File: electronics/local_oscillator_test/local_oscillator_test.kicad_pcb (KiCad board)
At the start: 2 copper layers, 0 parts

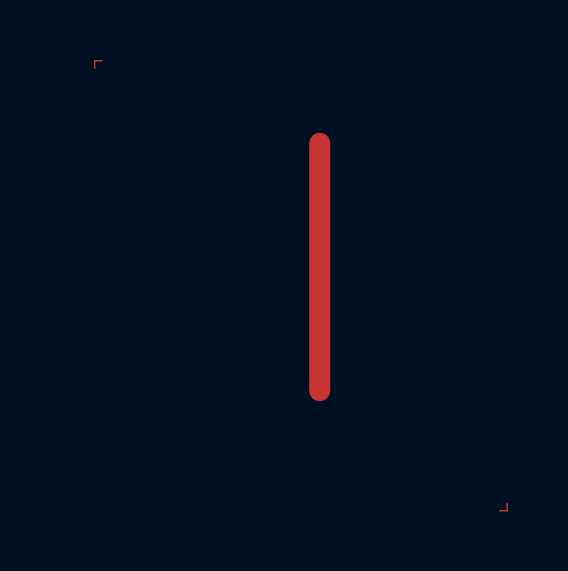
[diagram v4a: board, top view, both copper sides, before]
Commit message: Impulse functional, just needed to set ground plane
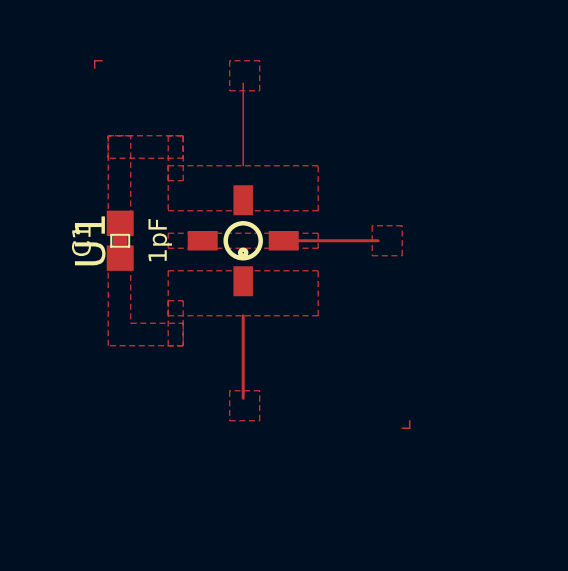
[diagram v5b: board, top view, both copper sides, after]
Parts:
- added C1: 1pF, 0402, F.Cu at (15.8, 18.5)
- added U1: CE3520K3, 0xDBFB7:4-Micro-X, F.Cu at (19.9, 18.5)
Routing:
- net (no net): track 9.25 -> 1.00 mm
- net /GATE: track 0.00 -> 3.91 mm
- net GND: track 0.00 -> 2.75 mm
- net /OSC1: track 0.00 -> 2.75 mm
- added copper zone on F.Cu, net /GATE
- added copper zone on F.Cu, net /OSC1
- added copper zone on F.Cu, net GND
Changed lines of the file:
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@@
     (thickness 1.6)
     (drawings 0)
-    (tracks 5)
+    (tracks 8)
     (zones 0)
-    (modules 0)
-    (nets 1)
+    (modules 2)
+    (nets 4)
   )
   (page A4)
@@
   )
   (net 0 "")
+  (net 1 /OSC1)
+  (net 2 GND)
+  (net 3 /GATE)
   (net_class Default "This is the default net class."
     (clearance 0.2)
@@
     (uvia_dia 0.3)
     (uvia_drill 0.1)
+    (add_net /GATE)
+    (add_net /OSC1)
+    (add_net GND)
+  )
+  (module 0xDBFB7:4-Micro-X (layer F.Cu)
+    (at 19.95 18.5 270)
+    (fp_text reference U1 (at 0 5.072 270) (layer F.SilkS)
+      (effects (font (size 1 1) (thickness 0.15)))
+    )
+    (fp_text value CE3520K3 (at 0 4.072 270) (layer F.Fab)
+      (effects (font (size 1 1) (thickness 0.15)))
+    )
+    (fp_text user Gate (at 1.4 -0.5 270) (layer Dwgs.User)
+      (effects (font (size 0.2 0.2) (thickness 0.05)))
+    )
+    (fp_text user Drain (at -1.3 -0.5 270) (layer Dwgs.User)
+      (effects (font (size 0.2 0.2) (thickness 0.05)))
+    )
+    (fp_text user Source (at -0.5 -1.3) (layer Dwgs.User)
+      (effects (font (size 0.2 0.2) (thickness 0.05)))
+    )
+    (fp_text user Source (at -0.5 1.4) (layer Dwgs.User)
+      (effects (font (size 0.2 0.2) (thickness 0.05)))
+    )
+    (fp_circle (center 0 0) (end 0.583095 0) (layer F.SilkS) (width 0.15))
+    (fp_circle (center 0.4 0) (end 0.5 0) (layer F.SilkS) (width 0.15))
+    (pad 2 smd rect (at -1.35 0) (size 0.65 1) (layers F.Cu F.Paste F.Mask)
+      (net 3 /GATE))
+    (pad 1 smd rect (at 0 -1.35 270) (size 0.65 1) (layers F.Cu F.Paste F.Mask)
+      (net 2 GND))
+    (pad 4 smd rect (at 1.35 0 180) (size 0.65 1) (layers F.Cu F.Paste F.Mask)
+      (net 3 /GATE))
+    (pad 3 smd rect (at 0 1.35 90) (size 0.65 1) (layers F.Cu F.Paste F.Mask)
+      (net 2 GND))
+  )
+  (module 0402 (layer F.Cu)
+    (at 15.85 18.5 90)
+    (descr "GENERIC 1005 (0402) PACKAGE")
+    (tags "GENERIC 1005 (0402) PACKAGE")
+    (attr smd)
+    (fp_text reference C1 (at 0 -1.27 90) (layer F.SilkS)
+      (effects (font (size 0.6096 0.6096) (thickness 0.127)))
+    )
+    (fp_text value 1pF (at 0 1.27 90) (layer F.SilkS)
+      (effects (font (size 0.6096 0.6096) (thickness 0.127)))
+    )
+    (fp_line (start -0.55372 0.3048) (end -0.254 0.3048) (layer Dwgs.User) (width 0.06604))
+    (fp_line (start -0.254 0.3048) (end -0.254 -0.3048) (layer Dwgs.User) (width 0.06604))
+    (fp_line (start -0.55372 -0.3048) (end -0.254 -0.3048) (layer Dwgs.User) (width 0.06604))
+    (fp_line (start -0.55372 0.3048) (end -0.55372 -0.3048) (layer Dwgs.User) (width 0.06604))
+    (fp_line (start 0.25654 0.3048) (end 0.5588 0.3048) (layer Dwgs.User) (width 0.06604))
+    (fp_line (start 0.5588 0.3048) (end 0.5588 -0.3048) (layer Dwgs.User) (width 0.06604))
+    (fp_line (start 0.25654 -0.3048) (end 0.5588 -0.3048) (layer Dwgs.User) (width 0.06604))
+    (fp_line (start 0.25654 0.3048) (end 0.25654 -0.3048) (layer Dwgs.User) (width 0.06604))
+    (fp_line (start -0.19812 0.29972) (end 0.19812 0.29972) (layer F.SilkS) (width 0.06604))
+    (fp_line (start 0.19812 0.29972) (end 0.19812 -0.29972) (layer F.SilkS) (width 0.06604))
+    (fp_line (start -0.19812 -0.29972) (end 0.19812 -0.29972) (layer F.SilkS) (width 0.06604))
+    (fp_line (start -0.19812 0.29972) (end -0.19812 -0.29972) (layer F.SilkS) (width 0.06604))
+    (fp_line (start -0.26924 -0.2286) (end 0.26924 -0.2286) (layer Dwgs.User) (width 0.1524))
+    (fp_line (start 0.26924 0.2286) (end -0.26924 0.2286) (layer Dwgs.User) (width 0.1524))
+    (fp_line (start -1.19888 -0.6477) (end 1.19888 -0.6477) (layer F.CrtYd) (width 0.0508))
+    (fp_line (start 1.19888 -0.6477) (end 1.19888 0.6477) (layer F.CrtYd) (width 0.0508))
+    (fp_line (start 1.19888 0.6477) (end -1.19888 0.6477) (layer F.CrtYd) (width 0.0508))
+    (fp_line (start -1.19888 0.6477) (end -1.19888 -0.6477) (layer F.CrtYd) (width 0.0508))
+    (pad 1 smd rect (at -0.57912 0 90) (size 0.84836 0.89916) (layers F.Cu F.Paste F.Mask)
+      (net 3 /GATE) (solder_mask_margin 0.1016))
+    (pad 2 smd rect (at 0.57912 0 90) (size 0.84836 0.89916) (layers F.Cu F.Paste F.Mask)
+      (net 3 /GATE) (solder_mask_margin 0.1016))
   )
   (segment (start 15 12.75) (end 15 12.5) (width 0.05) (layer F.Cu) (net 0))
   (segment (start 15 12.5) (end 15.25 12.5) (width 0.05) (layer F.Cu) (net 0))
-  (segment (start 28.75 27.25) (end 28.75 27.5) (width 0.05) (layer F.Cu) (net 0))
-  (segment (start 28.75 27.5) (end 28.5 27.5) (width 0.05) (layer F.Cu) (net 0))
-  (segment (start 22.5 15.25) (end 22.5 23.5) (width 0.7) (layer F.Cu) (net 0))
+  (segment (start 25.5 24.5) (end 25.5 24.75) (width 0.05) (layer F.Cu) (net 0))
+  (segment (start 25.5 24.75) (end 25.25 24.75) (width 0.05) (layer F.Cu) (net 0))
+  (segment (start 19.95 13.25) (end 19.95 16) (width 0.05) (layer F.Cu) (net 1))
+  (segment (start 24.45 18.5) (end 21.7 18.5) (width 0.1) (layer F.Cu) (net 2))
+  (segment (start 19.95 21) (end 19.95 23.75) (width 0.1) (layer F.Cu) (net 3))
+  (segment (start 15.85 17.92088) (end 15.85 19.07912) (width 0.5) (layer F.Cu) (net 3))
+  (zone (net 3) (net_name /GATE) (layer F.Cu) (hatch edge 0.508)
+    (connect_pads yes (clearance 0))
+    (min_thickness 0.254)
+    (fill yes (arc_segments 16) (thermal_gap 0) (thermal_bridge_width 0))
+    (polygon
+      (pts
+        (xy 15.45 15) (xy 15.45 18) (xy 16.2 18) (xy 16.2 15)
+      )
+    )
+  )
+  (zone (net 1) (net_name /OSC1) (layer F.Cu) (hatch edge 0.508)
+    (connect_pads yes (clearance 0))
+    (min_thickness 0.254)
+    (fill yes (arc_segments 16) (thermal_gap 0) (thermal_bridge_width 0))
+    (polygon
+      (pts
+        (xy 19.5 13.5) (xy 20.5 13.5) (xy 20.5 12.5) (xy 19.5 12.5)
+      )
+    )
+  )
+  (zone (net 1) (net_name /OSC1) (layer F.Cu) (hatch edge 0.508)
+    (connect_pads yes (clearance 0))
+    (min_thickness 0.254)
+    (fill yes (arc_segments 16) (thermal_gap 0) (thermal_bridge_width 0))
+    (polygon
+      (pts
+        (xy 17.95 16.5) (xy 17.95 15) (xy 17.45 15) (xy 17.45 16.5)
+      )
+    )
+  )
+  (zone (net 3) (net_name /GATE) (layer F.Cu) (hatch edge 0.508)
+    (connect_pads yes (clearance 0))
+    (min_thickness 0.254)
+    (fill yes (arc_segments 16) (thermal_gap 0) (thermal_bridge_width 0))
+    (polygon
+      (pts
+        (xy 17.95 22) (xy 15.45 22) (xy 15.45 19) (xy 16.2 19) (xy 16.2 21.25)
+        (xy 17.95 21.25)
+      )
+    )
+  )
+  (zone (net 2) (net_name GND) (layer F.Cu) (hatch edge 0.508)
+    (connect_pads yes (clearance 0))
+    (min_thickness 0.254)
+    (fill yes (arc_segments 16) (thermal_gap 0) (thermal_bridge_width 0))
+    (polygon
+      (pts
+        (xy 24.25 18) (xy 24.25 19) (xy 25.25 19) (xy 25.25 18)
+      )
+    )
+  )
+  (zone (net 2) (net_name GND) (layer F.Cu) (hatch edge 0.508)
+    (connect_pads yes (clearance 0))
+    (min_thickness 0.254)
+    (fill yes (arc_segments 16) (thermal_gap 0) (thermal_bridge_width 0))
+    (polygon
+      (pts
+        (xy 17.45 18.25) (xy 22.45 18.25) (xy 22.45 18.75) (xy 17.45 18.75)
+      )
+    )
+  )
+  (zone (net 1) (net_name /OSC1) (layer F.Cu) (hatch edge 0.508)
+    (connect_pads yes (clearance 0))
+    (min_thickness 0.254)
+    (fill yes (arc_segments 16) (thermal_gap 0) (thermal_bridge_width 0))
+    (polygon
+      (pts
+        (xy 17.95 15) (xy 17.95 15.75) (xy 15.45 15.75) (xy 15.45 15)
+      )
+    )
+  )
+  (zone (net 3) (net_name /GATE) (layer F.Cu) (hatch edge 0.508)
+    (connect_pads yes (clearance 0))
+    (min_thickness 0.254)
+    (fill yes (arc_segments 16) (thermal_gap 0) (thermal_bridge_width 0))
+    (polygon
+      (pts
+        (xy 20.5 23.5) (xy 19.5 23.5) (xy 19.5 24.5) (xy 20.5 24.5)
+      )
+    )
+  )
+  (zone (net 3) (net_name /GATE) (layer F.Cu) (hatch edge 0.508)
+    (connect_pads yes (clearance 0))
+    (min_thickness 0.254)
+    (fill yes (arc_segments 16) (thermal_gap 0) (thermal_bridge_width 0))
+    (polygon
+      (pts
+        (xy 17.95 20.5) (xy 17.95 22) (xy 17.45 22) (xy 17.45 20.5)
+      )
+    )
+  )
+  (zone (net 3) (net_name /GATE) (layer F.Cu) (hatch edge 0.508)
+    (connect_pads yes (clearance 0.508))
+    (min_thickness 0.254)
+    (fill yes (arc_segments 16) (thermal_gap 0.508) (thermal_bridge_width 0.508))
+    (polygon
+      (pts
+        (xy 22.45 21) (xy 22.45 19.5) (xy 17.45 19.5) (xy 17.45 21)
+      )
+    )
+  )
+  (zone (net 3) (net_name /GATE) (layer F.Cu) (hatch edge 0.508)
+    (connect_pads yes (clearance 0.508))
+    (min_thickness 0.254)
+    (fill yes (arc_segments 16) (thermal_gap 0.508) (thermal_bridge_width 0.508))
+    (polygon
+      (pts
+        (xy 22.45 17.5) (xy 22.45 16) (xy 17.45 16) (xy 17.45 17.5)
+      )
+    )
+  )
 )

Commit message: LO works!
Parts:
- added C2: 1pF, 0402, F.Cu at (17.0, 15.5)
- moved U1 3.38 mm to (23.2, 19.2)
- moved C1 2.45 mm to (18.2, 18.0)
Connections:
- C1 pad 2: /GATE -> Net-(C1-Pad2)
- U1 pad 2: /GATE -> /OSC1
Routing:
- net /GATE: track 3.91 -> 0.00 mm
- net GND: track 2.75 -> 0.00 mm
- net /OSC1: track 2.75 -> 0.00 mm
- removed copper zone on F.Cu, net /GATE
- removed copper zone on F.Cu, net /OSC1
- removed copper zone on F.Cu, net GND
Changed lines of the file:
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@@
     (thickness 1.6)
     (drawings 0)
-    (tracks 8)
+    (tracks 4)
     (zones 0)
-    (modules 2)
-    (nets 4)
+    (modules 3)
+    (nets 7)
   )
   (page A4)
@@
     (pad_drill 0.762)
     (pad_to_mask_clearance 0.2)
-    (aux_axis_origin 22.5 25)
-    (grid_origin 22.5 25)
+    (aux_axis_origin 15 12.5)
+    (grid_origin 15 12.5)
     (visible_elements FEFFFF7F)
     (pcbplotparams
@@
   )
   (net 0 "")
-  (net 1 /OSC1)
-  (net 2 GND)
-  (net 3 /GATE)
+  (net 1 "Net-(C1-Pad2)")
+  (net 2 /OSC1)
+  (net 3 GND)
+  (net 4 /GATE)
+  (net 5 "Net-(C2-Pad1)")
+  (net 6 "Net-(C2-Pad2)")
   (net_class Default "This is the default net class."
     (clearance 0.2)
@@
     (add_net /OSC1)
     (add_net GND)
+    (add_net "Net-(C1-Pad2)")
+    (add_net "Net-(C2-Pad1)")
+    (add_net "Net-(C2-Pad2)")
+  )
+  (module 0402 (layer F.Cu)
+    (at 17 15.5)
+    (descr "GENERIC 1005 (0402) PACKAGE")
+    (tags "GENERIC 1005 (0402) PACKAGE")
+    (attr smd)
+    (fp_text reference C2 (at 0 -1.27) (layer F.SilkS)
+      (effects (font (size 0.6096 0.6096) (thickness 0.127)))
+    )
+    (fp_text value 1pF (at 0 1.27) (layer F.SilkS)
+      (effects (font (size 0.6096 0.6096) (thickness 0.127)))
+    )
+    (fp_line (start -0.55372 0.3048) (end -0.254 0.3048) (layer Dwgs.User) (width 0.06604))
+    (fp_line (start -0.254 0.3048) (end -0.254 -0.3048) (layer Dwgs.User) (width 0.06604))
+    (fp_line (start -0.55372 -0.3048) (end -0.254 -0.3048) (layer Dwgs.User) (width 0.06604))
+    (fp_line (start -0.55372 0.3048) (end -0.55372 -0.3048) (layer Dwgs.User) (width 0.06604))
+    (fp_line (start 0.25654 0.3048) (end 0.5588 0.3048) (layer Dwgs.User) (width 0.06604))
+    (fp_line (start 0.5588 0.3048) (end 0.5588 -0.3048) (layer Dwgs.User) (width 0.06604))
+    (fp_line (start 0.25654 -0.3048) (end 0.5588 -0.3048) (layer Dwgs.User) (width 0.06604))
+    (fp_line (start 0.25654 0.3048) (end 0.25654 -0.3048) (layer Dwgs.User) (width 0.06604))
+    (fp_line (start -0.19812 0.29972) (end 0.19812 0.29972) (layer F.SilkS) (width 0.06604))
+    (fp_line (start 0.19812 0.29972) (end 0.19812 -0.29972) (layer F.SilkS) (width 0.06604))
+    (fp_line (start -0.19812 -0.29972) (end 0.19812 -0.29972) (layer F.SilkS) (width 0.06604))
+    (fp_line (start -0.19812 0.29972) (end -0.19812 -0.29972) (layer F.SilkS) (width 0.06604))
+    (fp_line (start -0.26924 -0.2286) (end 0.26924 -0.2286) (layer Dwgs.User) (width 0.1524))
+    (fp_line (start 0.26924 0.2286) (end -0.26924 0.2286) (layer Dwgs.User) (width 0.1524))
+    (fp_line (start -1.19888 -0.6477) (end 1.19888 -0.6477) (layer F.CrtYd) (width 0.0508))
+    (fp_line (start 1.19888 -0.6477) (end 1.19888 0.6477) (layer F.CrtYd) (width 0.0508))
+    (fp_line (start 1.19888 0.6477) (end -1.19888 0.6477) (layer F.CrtYd) (width 0.0508))
+    (fp_line (start -1.19888 0.6477) (end -1.19888 -0.6477) (layer F.CrtYd) (width 0.0508))
+    (pad 1 smd rect (at -0.57912 0) (size 0.84836 0.89916) (layers F.Cu F.Paste F.Mask)
+      (net 5 "Net-(C2-Pad1)") (solder_mask_margin 0.1016))
+    (pad 2 smd rect (at 0.57912 0) (size 0.84836 0.89916) (layers F.Cu F.Paste F.Mask)
+      (net 6 "Net-(C2-Pad2)") (solder_mask_margin 0.1016))
   )
   (module 0xDBFB7:4-Micro-X (layer F.Cu)
-    (at 19.95 18.5 270)
+    (at 23.25 19.25 270)
     (fp_text reference U1 (at 0 5.072 270) (layer F.SilkS)
       (effects (font (size 1 1) (thickness 0.15)))
     )
-    (fp_text value CE3520K3 (at 0 4.072 270) (layer F.Fab)
+    (fp_text value CE3520K3 (at 0.25 -4.25 270) (layer F.Fab)
       (effects (font (size 1 1) (thickness 0.15)))
     )
@@
     (fp_circle (center 0.4 0) (end 0.5 0) (layer F.SilkS) (width 0.15))
     (pad 2 smd rect (at -1.35 0) (size 0.65 1) (layers F.Cu F.Paste F.Mask)
-      (net 3 /GATE))
+      (net 2 /OSC1))
     (pad 1 smd rect (at 0 -1.35 270) (size 0.65 1) (layers F.Cu F.Paste F.Mask)
-      (net 2 GND))
+      (net 3 GND))
     (pad 4 smd rect (at 1.35 0 180) (size 0.65 1) (layers F.Cu F.Paste F.Mask)
-      (net 3 /GATE))
+      (net 4 /GATE))
     (pad 3 smd rect (at 0 1.35 90) (size 0.65 1) (layers F.Cu F.Paste F.Mask)
-      (net 2 GND))
+      (net 3 GND))
   )
   (module 0402 (layer F.Cu)
-    (at 15.85 18.5 90)
+    (at 18.25 18 90)
     (descr "GENERIC 1005 (0402) PACKAGE")
     (tags "GENERIC 1005 (0402) PACKAGE")
@@
     (fp_line (start -1.19888 0.6477) (end -1.19888 -0.6477) (layer F.CrtYd) (width 0.0508))
     (pad 1 smd rect (at -0.57912 0 90) (size 0.84836 0.89916) (layers F.Cu F.Paste F.Mask)
-      (net 3 /GATE) (solder_mask_margin 0.1016))
+      (net 4 /GATE) (solder_mask_margin 0.1016))
     (pad 2 smd rect (at 0.57912 0 90) (size 0.84836 0.89916) (layers F.Cu F.Paste F.Mask)
-      (net 3 /GATE) (solder_mask_margin 0.1016))
+      (net 1 "Net-(C1-Pad2)") (solder_mask_margin 0.1016))
   )
   (segment (start 15 12.75) (end 15 12.5) (width 0.05) (layer F.Cu) (net 0))
@@
   (segment (start 25.5 24.5) (end 25.5 24.75) (width 0.05) (layer F.Cu) (net 0))
   (segment (start 25.5 24.75) (end 25.25 24.75) (width 0.05) (layer F.Cu) (net 0))
-  (segment (start 19.95 13.25) (end 19.95 16) (width 0.05) (layer F.Cu) (net 1))
-  (segment (start 24.45 18.5) (end 21.7 18.5) (width 0.1) (layer F.Cu) (net 2))
-  (segment (start 19.95 21) (end 19.95 23.75) (width 0.1) (layer F.Cu) (net 3))
-  (segment (start 15.85 17.92088) (end 15.85 19.07912) (width 0.5) (layer F.Cu) (net 3))
-  (zone (net 3) (net_name /GATE) (layer F.Cu) (hatch edge 0.508)
-    (connect_pads yes (clearance 0))
-    (min_thickness 0.254)
-    (fill yes (arc_segments 16) (thermal_gap 0) (thermal_bridge_width 0))
-    (polygon
-      (pts
-        (xy 15.45 15) (xy 15.45 18) (xy 16.2 18) (xy 16.2 15)
-      )
-    )
-  )
-  (zone (net 1) (net_name /OSC1) (layer F.Cu) (hatch edge 0.508)
-    (connect_pads yes (clearance 0))
-    (min_thickness 0.254)
-    (fill yes (arc_segments 16) (thermal_gap 0) (thermal_bridge_width 0))
-    (polygon
-      (pts
-        (xy 19.5 13.5) (xy 20.5 13.5) (xy 20.5 12.5) (xy 19.5 12.5)
-      )
-    )
-  )
-  (zone (net 1) (net_name /OSC1) (layer F.Cu) (hatch edge 0.508)
-    (connect_pads yes (clearance 0))
-    (min_thickness 0.254)
-    (fill yes (arc_segments 16) (thermal_gap 0) (thermal_bridge_width 0))
-    (polygon
-      (pts
-        (xy 17.95 16.5) (xy 17.95 15) (xy 17.45 15) (xy 17.45 16.5)
-      )
-    )
-  )
-  (zone (net 3) (net_name /GATE) (layer F.Cu) (hatch edge 0.508)
-    (connect_pads yes (clearance 0))
-    (min_thickness 0.254)
-    (fill yes (arc_segments 16) (thermal_gap 0) (thermal_bridge_width 0))
-    (polygon
-      (pts
-        (xy 17.95 22) (xy 15.45 22) (xy 15.45 19) (xy 16.2 19) (xy 16.2 21.25)
-        (xy 17.95 21.25)
-      )
-    )
-  )
-  (zone (net 2) (net_name GND) (layer F.Cu) (hatch edge 0.508)
-    (connect_pads yes (clearance 0))
-    (min_thickness 0.254)
-    (fill yes (arc_segments 16) (thermal_gap 0) (thermal_bridge_width 0))
-    (polygon
-      (pts
-        (xy 24.25 18) (xy 24.25 19) (xy 25.25 19) (xy 25.25 18)
-      )
-    )
-  )
-  (zone (net 2) (net_name GND) (layer F.Cu) (hatch edge 0.508)
-    (connect_pads yes (clearance 0))
-    (min_thickness 0.254)
-    (fill yes (arc_segments 16) (thermal_gap 0) (thermal_bridge_width 0))
-    (polygon
-      (pts
-        (xy 17.45 18.25) (xy 22.45 18.25) (xy 22.45 18.75) (xy 17.45 18.75)
-      )
-    )
-  )
-  (zone (net 1) (net_name /OSC1) (layer F.Cu) (hatch edge 0.508)
-    (connect_pads yes (clearance 0))
-    (min_thickness 0.254)
-    (fill yes (arc_segments 16) (thermal_gap 0) (thermal_bridge_width 0))
-    (polygon
-      (pts
-        (xy 17.95 15) (xy 17.95 15.75) (xy 15.45 15.75) (xy 15.45 15)
-      )
-    )
-  )
-  (zone (net 3) (net_name /GATE) (layer F.Cu) (hatch edge 0.508)
-    (connect_pads yes (clearance 0))
-    (min_thickness 0.254)
-    (fill yes (arc_segments 16) (thermal_gap 0) (thermal_bridge_width 0))
-    (polygon
-      (pts
-        (xy 20.5 23.5) (xy 19.5 23.5) (xy 19.5 24.5) (xy 20.5 24.5)
-      )
-    )
-  )
-  (zone (net 3) (net_name /GATE) (layer F.Cu) (hatch edge 0.508)
-    (connect_pads yes (clearance 0))
-    (min_thickness 0.254)
-    (fill yes (arc_segments 16) (thermal_gap 0) (thermal_bridge_width 0))
-    (polygon
-      (pts
-        (xy 17.95 20.5) (xy 17.95 22) (xy 17.45 22) (xy 17.45 20.5)
-      )
-    )
-  )
-  (zone (net 3) (net_name /GATE) (layer F.Cu) (hatch edge 0.508)
-    (connect_pads yes (clearance 0.508))
-    (min_thickness 0.254)
-    (fill yes (arc_segments 16) (thermal_gap 0.508) (thermal_bridge_width 0.508))
-    (polygon
-      (pts
-        (xy 22.45 21) (xy 22.45 19.5) (xy 17.45 19.5) (xy 17.45 21)
-      )
-    )
-  )
-  (zone (net 3) (net_name /GATE) (layer F.Cu) (hatch edge 0.508)
-    (connect_pads yes (clearance 0.508))
-    (min_thickness 0.254)
-    (fill yes (arc_segments 16) (thermal_gap 0.508) (thermal_bridge_width 0.508))
-    (polygon
-      (pts
-        (xy 22.45 17.5) (xy 22.45 16) (xy 17.45 16) (xy 17.45 17.5)
-      )
-    )
-  )
 )
